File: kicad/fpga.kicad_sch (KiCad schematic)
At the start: 83 parts, among them U1 XC7A50T-2CSG325I

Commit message: Update Odin hardware design, imported parts, and documentation
Include EasyEDA symbols, footprints and 3D models; revise FPGA allocation, power and extension buses; add qualification audits and user documentation.

Validation: EasyEDA audit, qualified parts, power budget and Python syntax pass. KiCad ERC reports 1 error and 319 warnings; DRC reports 90 violations, 499 unconnected items and 209 schematic parity issues. This is a work-in-progress design snapshot. Imported vendor assets retain their original formatting.
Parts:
- added C100, C101, C102, C103, C104, C105, C106, C107, C108, C109, C110, C111, C98, C99: 4.7uF, Capacitor_SMD:C_0603_1608Metric, symbol Device:C
- added C75, C76, C77, C78, C79, C80, C81, C82, C83, C84, C85, C86, C87, C88, C89, C90, C91, C92, C93, C94, C95, C96, C97: 100nF, Capacitor_SMD:C_0402_1005Metric, symbol Device:C
- added unit 8 of U1
- added unit 9 of U1
- added unit 10 of U1
- added unit 11 of U1
- C1, C10, C11, C12, C13, C14, C15, C16, C17, C18, C19, C2, C20, C21, C22, C23, C24, C25, C26, C27, C28, C29, C3, C30, C31, C32, C33, C34, C35, C36, C37, C38, C39, C4, C40, C41, C42, C43, C44, C45, C46, C47, C48, C49, C5, C50, C51, C52, C53, C54, C55, C56, C57, C58, C59, C6, C60, C7, C8, C9: LCSC (none) -> C1525
- C61, C62, C63, C64, C65, C66, C67, C68, C69, C70, C71, C72, C73, C74: value 4.7uF -> 100nF; footprint Capacitor_SMD:C_0603_1608Metric -> Capacitor_SMD:C_0402_1005Metric; LCSC (none) -> C1525
- D1: value green -> F.0603.00025/P2-0603G1TS2-06T-002; footprint LED_SMD:LED_0603_1608Metric -> EasyEDA:LED0603-RD_GREEN; symbol Device:LED -> EasyEDA:F.0603.00025_P2-0603G1TS2-06T-002; LCSC (none) -> C7496818
- R1, R2, R3, R4, R5, R6: LCSC (none) -> C25900
- U1: value XC7A50T-2CSG325I -> XC7A100T-2FGG676I; footprint odin:BGA-324_15x15mm_Layout18x18_P0.8mm -> EasyEDA:FBGA-676_L27.0-W27.0-R26-C26-P1.00-BL; symbol odin:XC7A50T-2CSG325I -> odin:XC7A100T-2FGG676I; LCSC (none) -> C1521803
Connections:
- net +1V0: now also C32.1, C33.1, C34.1, C35.1, C36.1, C37.1, C38.1, C39.1, C40.1, C46.1, C47.1, C48.1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; no longer C11.1, C12.1, C13.1, C14.1, C15.1, C16.1, C17.1, C18.1, C19.1, C20.1, C21.1, C22.1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
- net +1V0_MGT: now also C10.1, C11.1, C12.1, C13.1, C14.1, C15.1, C6.1, C7.1, C8.1, C9.1, C110.1, U1.AA10 (MGTAVCC_G10)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; no longer C32.1, C33.1, C34.1, C35.1, C73.1, U1.B4 (MGTAVCC), U1.C5 (MGTAVCC), U1.E5 (MGTAVCC), U1.F5 (MGTAVCC)
- net +1V2_MGT: now also C16.1, C17.1, C18.1, C19.1, C20.1, C21.1, C22.1, C23.1, C24.1, C25.1, C26.1, C27.1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; no longer C36.1, C37.1, C38.1, C39.1, C40.1, C74.1, U1.A2 (MGTAVTT), U1.C1 (MGTAVTT), U1.E1 (MGTAVTT), U1.F3 (MGTAVTT), U1.G2 (MGTAVTT)
- net +1V8: now also C41.1, C42.1, C43.1, C44.1, C45.1, U1.M12 (VCCADC_0), U1.P12 (VREFP_0), C102.1, C103.1, U1.J9 (VCCAUX), U1.L9 (VCCAUX), U1.N9 (VCCAUX)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; no longer C10.1, C6.1, C65.1, C66.1, C7.1, C8.1, C9.1, U1.G12 (VCCAUX), U1.H13 (VCCAUX), U1.J10 (VCCADC_0), U1.K13 (VCCAUX), U1.L10 (VREFP_0)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
- net +3V3: now also C50.1, C51.1, C52.1, C53.1, C54.1, C55.1, C56.1, C57.1, C58.1, C59.1, C60.1, C61.1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; no longer C41.1, C42.1, C43.1, C44.1, C45.1, C46.1, C47.1, C68.1, U1.E10 (VCCO_0), U1.E12 (CFGBVS_0), U1.L16 (VCCO_14), U1.P17 (VCCO_14)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
- net CFG_CCLK: now also U1.H13 (CCLK_0); no longer U1.E8 (CCLK_0)
- net CFG_DONE: now also U1.W10 (DONE_0); no longer U1.F12 (DONE_0)
- net CFG_INIT_B: now also U1.V11 (INIT_B_0); no longer U1.T10 (INIT_B_0)
- net CFG_M0: now also U1.AB7 (M0_0); no longer U1.R12 (M0_0)
- net CFG_M1: now also U1.Y9 (M1_0); no longer U1.R11 (M1_0)
- net CFG_M2: now also U1.W9 (M2_0); no longer U1.F13 (M2_0)
- net CFG_PROG_B: now also U1.AE16 (PROGRAM_B_0); no longer U1.P10 (PROGRAM_B_0)
- net DBG_TCK: now also U1.P23 (IO_L17P_T2_A14_D30_14); no longer U1.U15 (IO_L17P_T2_A14_D30_14)
- net DBG_TDI: now also U1.R20 (IO_L18P_T2_A12_D28_14); no longer U1.V16 (IO_L18P_T2_A12_D28_14)
- net DBG_TDO: now also U1.R21 (IO_L18N_T2_A11_D27_14); no longer U1.V17 (IO_L18N_T2_A11_D27_14)
- net DBG_TMS: now also U1.P24 (IO_L17N_T2_A13_D29_14); no longer U1.U16 (IO_L17N_T2_A13_D29_14)
- net FLASH_CS_B: now also U1.P18 (IO_L6P_T0_FCS_B_14); no longer U1.L15 (IO_L6P_T0_FCS_B_14)
- net FLASH_D0_MOSI: now also U1.R14 (IO_L1P_T0_D00_MOSI_14); no longer U1.K16 (IO_L1P_T0_D00_MOSI_14)
- net FLASH_D1_MISO: now also U1.R15 (IO_L1N_T0_D01_DIN_14); no longer U1.L17 (IO_L1N_T0_D01_DIN_14)
- net FLASH_D2_WP: now also U1.P14 (IO_L2P_T0_D02_14); no longer U1.J15 (IO_L2P_T0_D02_14)
- net FLASH_D3_HOLD: now also U1.N14 (IO_L2N_T0_D03_14); no longer U1.J16 (IO_L2N_T0_D03_14)
- net FPGA_DXN: now also U1.R11 (DXN_0); no longer U1.M9 (DXN_0)
- net FPGA_DXP: now also U1.R12 (DXP_0); no longer U1.M10 (DXP_0)
- net GND: now also U1.G14 (VCCBATT_0), U1.M11 (GNDADC_0), U1.N11 (VREFN_0), U1.N12 (VP_0), U1.P11 (VN_0), C100.2, C101.2, C102.2, C103.2, C104.2, C105.2, C106.2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; no longer U1.A1 (GND), U1.A11 (GND), U1.A18 (GND), U1.A5 (GND), U1.A7 (GND), U1.A8 (GND), U1.B18 (GND), U1.B3 (GND), U1.B7 (GND), U1.B8 (GND), U1.C15 (GND), U1.C2 (GND)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
- net JTAG_TCK: now also U1.H12 (TCK_0); no longer U1.F8 (TCK_0)
- net JTAG_TDI: now also U1.H10 (TDI_0); no longer U1.T9 (TDI_0)
- net JTAG_TDO: now also U1.J10 (TDO_0); no longer U1.T8 (TDO_0)
- net JTAG_TMS: now also U1.H11 (TMS_0); no longer U1.R8 (TMS_0)
- net MGTPRXN0: now also U1.A11 (MGTPRXN0_216); no longer U1.E3 (MGTPRXN0_216)
- net MGTPRXN1: now also U1.C14 (MGTPRXN1_216); no longer U1.A3 (MGTPRXN1_216)
- net MGTPRXP0: now also U1.B11 (MGTPRXP0_216); no longer U1.E4 (MGTPRXP0_216)
- net MGTPRXP1: now also U1.D14 (MGTPRXP1_216); no longer U1.A4 (MGTPRXP1_216)
- net MGTPTXN0: now also U1.A7 (MGTPTXN0_216); no longer U1.H1 (MGTPTXN0_216)
- net MGTPTXN1: now also U1.C8 (MGTPTXN1_216); no longer U1.F1 (MGTPTXN1_216)
- net MGTPTXP0: now also U1.B7 (MGTPTXP0_216); no longer U1.H2 (MGTPTXP0_216)
- net MGTPTXP1: now also U1.D8 (MGTPTXP1_216); no longer U1.F2 (MGTPTXP1_216)
- net MGTREFCLK0N: now also U1.E11 (MGTREFCLK0N_216); no longer U1.D5 (MGTREFCLK0N_216)
- net MGTREFCLK0P: now also U1.F11 (MGTREFCLK0P_216); no longer U1.D6 (MGTREFCLK0P_216)
- net MGTRREF: now also U1.A15 (MGTRREF_216); no longer U1.A6 (MGTRREF_216)
- net PSRAM0_CE_B: now also U1.N17 (IO_L4N_T0_D05_14); no longer U1.L18 (IO_L4N_T0_D05_14)
- net PSRAM0_IO0: now also U1.R16 (IO_L5P_T0_D06_14); no longer U1.J14 (IO_L5P_T0_D06_14)
- net PSRAM0_IO1: now also U1.R17 (IO_L5N_T0_D07_14); no longer U1.K15 (IO_L5N_T0_D07_14)
- net PSRAM0_IO2: now also U1.K25 (IO_L7P_T1_D09_14); no longer U1.M16 (IO_L7P_T1_D09_14)
- net PSRAM0_IO3: now also U1.K26 (IO_L7N_T1_D10_14); no longer U1.M17 (IO_L7N_T1_D10_14)
- net PSRAM0_SCK: now also U1.N16 (IO_L4P_T0_D04_14); no longer U1.K17 (IO_L4P_T0_D04_14)
- net PSRAM1_CE_B: now also U1.L20 (IO_L8N_T1_D12_14); no longer U1.N14 (IO_L8N_T1_D12_14)
- net PSRAM1_IO0: now also U1.L24 (IO_L9P_T1_DQS_14); no longer U1.N16 (IO_L9P_T1_DQS_14)
- net PSRAM1_IO1: now also U1.L25 (IO_L9N_T1_DQS_D13_14); no longer U1.N17 (IO_L9N_T1_DQS_D13_14)
- net PSRAM1_IO2: now also U1.M24 (IO_L10P_T1_D14_14); no longer U1.N18 (IO_L10P_T1_D14_14)
- net PSRAM1_IO3: now also U1.M25 (IO_L10N_T1_D15_14); no longer U1.P18 (IO_L10N_T1_D15_14)
- net PSRAM1_SCK: now also U1.M20 (IO_L8P_T1_D11_14); no longer U1.M14 (IO_L8P_T1_D11_14)
- net PSRAM2_CE_B: now also U1.L23 (IO_L11N_T1_SRCC_14); no longer U1.P16 (IO_L11N_T1_SRCC_14)
- net PSRAM2_IO0: now also U1.M21 (IO_L12P_T1_MRCC_14); no longer U1.P14 (IO_L12P_T1_MRCC_14)
- net PSRAM2_IO1: now also U1.M22 (IO_L12N_T1_MRCC_14); no longer U1.R15 (IO_L12N_T1_MRCC_14)
- net PSRAM2_IO2: now also U1.N21 (IO_L13P_T2_MRCC_14); no longer U1.T14 (IO_L13P_T2_MRCC_14)
- net PSRAM2_IO3: now also U1.N22 (IO_L13N_T2_MRCC_14); no longer U1.T15 (IO_L13N_T2_MRCC_14)
- net PSRAM2_SCK: now also U1.L22 (IO_L11P_T1_SRCC_14); no longer U1.P15 (IO_L11P_T1_SRCC_14)
- net PSRAM3_CE_B: now also U1.P21 (IO_L14N_T2_SRCC_14); no longer U1.R17 (IO_L14N_T2_SRCC_14)
- net PSRAM3_IO0: now also U1.N23 (IO_L15P_T2_DQS_RDWR_B_14); no longer U1.R18 (IO_L15P_T2_DQS_RDWR_B_14)
- net PSRAM3_IO1: now also U1.N24 (IO_L15N_T2_DQS_DOUT_CSO_B_14); no longer U1.T18 (IO_L15N_T2_DQS_DOUT_CSO_B_14)
- net PSRAM3_IO2: now also U1.P19 (IO_L16P_T2_CSI_B_14); no longer U1.T17 (IO_L16P_T2_CSI_B_14)
- net PSRAM3_IO3: now also U1.N19 (IO_L16N_T2_A15_D31_14); no longer U1.U17 (IO_L16N_T2_A15_D31_14)
- net PSRAM3_SCK: now also U1.P20 (IO_L14P_T2_SRCC_14); no longer U1.R16 (IO_L14P_T2_SRCC_14)
- net PUDC_B: now also U1.P15 (IO_L3P_T0_DQS_PUDC_B_14); no longer U1.J18 (IO_L3P_T0_DQS_PUDC_B_14)
- net SB_UART_RX: now also U1.R25 (IO_L19P_T3_A10_D26_14); no longer U1.R13 (IO_L19P_T3_A10_D26_14)
- net SB_UART_TX: now also U1.P25 (IO_L19N_T3_A09_D25_VREF_14); no longer U1.T13 (IO_L19N_T3_A09_D25_VREF_14)
- net VCCIO_1: now also C68.1, C71.1, C72.1, C73.1, U1.F26 (VCCO_15), U1.G23 (VCCO_15), U1.H20 (VCCO_15), U1.J17 (VCCO_15), U1.K14 (VCCO_15), U1.M18 (VCCO_15), C106.1, C107.1; no longer C48.1, C49.1, C50.1, C51.1, C52.1, C53.1, C54.1, U1.A16 (VCCO_15), U1.B13 (VCCO_15), U1.C10 (VCCO_15), U1.D17 (VCCO_15), U1.E14 (VCCO_15)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
- net VCCIO_2: now also U1.K4 (VCCO_34), U1.L1 (VCCO_34), U1.M8 (VCCO_34), U1.N5 (VCCO_34), U1.P2 (VCCO_34), U1.T6 (VCCO_34), C108.1, C109.1, C86.1, C87.1, C88.1, C89.1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; no longer C55.1, C56.1, C57.1, C58.1, C59.1, C60.1, C71.1, C72.1, U1.L6 (VCCO_34), U1.M3 (VCCO_34), U1.P7 (VCCO_34), U1.R4 (VCCO_34)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
- removed net MGTPRXN2: U1.C3 (MGTPRXN2_216)
- removed net MGTPRXN3: U1.G3 (MGTPRXN3_216)
- removed net MGTPRXP2: U1.C4 (MGTPRXP2_216)
- removed net MGTPRXP3: U1.G4 (MGTPRXP3_216)
- removed net MGTPTXN2: U1.D1 (MGTPTXN2_216)
- removed net MGTPTXN3: U1.B1 (MGTPTXN3_216)
- removed net MGTPTXP2: U1.D2 (MGTPTXP2_216)
- removed net MGTPTXP3: U1.B2 (MGTPTXP3_216)
- removed net MGTREFCLK1N: U1.B5 (MGTREFCLK1N_216)
- removed net MGTREFCLK1P: U1.B6 (MGTREFCLK1P_216)
- removed net SLOTA_P0_N: U1.C8 (IO_L1N_T0_AD0N_15)
- removed net SLOTA_P0_P: U1.D8 (IO_L1P_T0_AD0P_15)
- removed net SLOTA_P1_N: U1.C9 (IO_L2N_T0_AD8N_15)
- removed net SLOTA_P1_P: U1.D9 (IO_L2P_T0_AD8P_15)
- removed net SLOTA_P2_N: U1.A9 (IO_L3N_T0_DQS_AD1N_15)
- removed net SLOTA_P2_P: U1.B9 (IO_L3P_T0_DQS_AD1P_15)
- removed net SLOTA_P3_N: U1.B11 (IO_L4N_T0_15)
- removed net SLOTA_P3_P: U1.C11 (IO_L4P_T0_15)
- removed net SLOTA_P4_N: U1.A10 (IO_L5N_T0_AD9N_15)
- removed net SLOTA_P4_P: U1.B10 (IO_L5P_T0_AD9P_15)
- removed net SLOTB_P0_N: U1.C12 (IO_L6N_T0_VREF_15)
- removed net SLOTB_P0_P: U1.D11 (IO_L6P_T0_15)
- removed net SLOTB_P1_N: U1.A12 (IO_L7N_T1_AD2N_15)
- removed net SLOTB_P1_P: U1.B12 (IO_L7P_T1_AD2P_15)
- removed net SLOTB_P2_N: U1.A14 (IO_L8N_T1_AD10N_15)
- removed net SLOTB_P2_P: U1.A13 (IO_L8P_T1_AD10P_15)
- removed net SLOTB_P3_N: U1.B15 (IO_L9N_T1_DQS_AD3N_15)
- removed net SLOTB_P3_P: U1.C14 (IO_L9P_T1_DQS_AD3P_15)
- removed net SLOTB_P4_N: U1.A15 (IO_L10N_T1_AD11N_15)
- removed net SLOTB_P4_P: U1.B14 (IO_L10P_T1_AD11P_15)
- removed net SLOTC_P0_N: U1.C13 (IO_L11N_T1_SRCC_15)
- removed net SLOTC_P0_P: U1.D13 (IO_L11P_T1_SRCC_15)
- removed net SLOTC_P1_N: U1.D14 (IO_L12N_T1_MRCC_15)
- removed net SLOTC_P1_P: U1.E13 (IO_L12P_T1_MRCC_15)
- removed net SLOTC_P2_N: U1.D15 (IO_L13N_T2_MRCC_15)
- removed net SLOTC_P2_P: U1.E15 (IO_L13P_T2_MRCC_15)
- removed net SLOTC_P3_N: U1.D16 (IO_L14N_T2_SRCC_15)
- removed net SLOTC_P3_P: U1.E16 (IO_L14P_T2_SRCC_15)
- removed net SLOTC_P4_N: U1.A17 (IO_L15N_T2_DQS_ADV_B_15)
- removed net SLOTC_P4_P: U1.B16 (IO_L15P_T2_DQS_15)
- removed net SLOTD_P0_N: U1.B17 (IO_L16N_T2_A27_15)
- removed net SLOTD_P0_P: U1.C16 (IO_L16P_T2_A28_15)
- removed net SLOTD_P1_N: U1.D18 (IO_L17N_T2_A25_15)
- removed net SLOTD_P1_P: U1.E17 (IO_L17P_T2_A26_15)
- removed net SLOTD_P2_N: U1.C18 (IO_L18N_T2_A23_15)
- removed net SLOTD_P2_P: U1.C17 (IO_L18P_T2_A24_15)
- removed net SLOTD_P3_N: U1.F18 (IO_L19N_T3_A21_VREF_15)
- removed net SLOTD_P3_P: U1.G17 (IO_L19P_T3_A22_15)
- removed net SLOTD_P4_N: U1.G16 (IO_L20N_T3_A19_15)
- removed net SLOTD_P4_P: U1.H16 (IO_L20P_T3_A20_15)
- removed net SLOTE_P0_N: U1.K5 (IO_L1N_T0_34)
- removed net SLOTE_P0_P: U1.K6 (IO_L1P_T0_34)
- removed net SLOTE_P1_N: U1.J4 (IO_L2N_T0_34)
- removed net SLOTE_P1_P: U1.J5 (IO_L2P_T0_34)
- removed net SLOTE_P2_N: U1.K1 (IO_L3N_T0_DQS_34)
- removed net SLOTE_P2_P: U1.K2 (IO_L3P_T0_DQS_34)
- removed net SLOTE_P3_N: U1.L2 (IO_L4N_T0_34)
- removed net SLOTE_P3_P: U1.K3 (IO_L4P_T0_34)
- removed net SLOTE_P4_N: U1.L3 (IO_L5N_T0_34)
- removed net SLOTE_P4_P: U1.L4 (IO_L5P_T0_34)
- removed net SLOTF_P0_N: U1.M5 (IO_L6N_T0_VREF_34)
- removed net SLOTF_P0_P: U1.L5 (IO_L6P_T0_34)
- removed net SLOTF_P1_N: U1.M1 (IO_L7N_T1_34)
- removed net SLOTF_P1_P: U1.M2 (IO_L7P_T1_34)
- removed net SLOTF_P2_N: U1.N6 (IO_L8N_T1_34)
- removed net SLOTF_P2_P: U1.M6 (IO_L8P_T1_34)
- removed net SLOTF_P3_N: U1.P1 (IO_L9N_T1_DQS_34)
- removed net SLOTF_P3_P: U1.N1 (IO_L9P_T1_DQS_34)
- removed net SLOTF_P4_N: U1.N4 (IO_L10N_T1_34)
- removed net SLOTF_P4_P: U1.M4 (IO_L10P_T1_34)
- removed net SLOTG_P0_N: U1.N2 (IO_L11N_T1_SRCC_34)
- removed net SLOTG_P0_P: U1.N3 (IO_L11P_T1_SRCC_34)
- removed net SLOTG_P1_N: U1.P3 (IO_L12N_T1_MRCC_34)
- removed net SLOTG_P1_P: U1.P4 (IO_L12P_T1_MRCC_34)
- removed net SLOTG_P2_N: U1.R1 (IO_L13N_T2_MRCC_34)
- removed net SLOTG_P2_P: U1.R2 (IO_L13P_T2_MRCC_34)
- removed net SLOTG_P3_N: U1.T2 (IO_L14N_T2_SRCC_34)
- removed net SLOTG_P3_P: U1.R3 (IO_L14P_T2_SRCC_34)
- removed net SLOTG_P4_N: U1.U1 (IO_L15N_T2_DQS_34)
- removed net SLOTG_P4_P: U1.U2 (IO_L15P_T2_DQS_34)
- removed net SLOTH_P0_N: U1.V2 (IO_L16N_T2_34)
- removed net SLOTH_P0_P: U1.V3 (IO_L16P_T2_34)
- removed net SLOTH_P1_N: U1.T3 (IO_L17N_T2_34)
- removed net SLOTH_P1_P: U1.T4 (IO_L17P_T2_34)
- removed net SLOTH_P2_N: U1.V4 (IO_L18N_T2_34)
- removed net SLOTH_P2_P: U1.U4 (IO_L18P_T2_34)
- removed net SLOTH_P3_N: U1.P5 (IO_L19N_T3_VREF_34)
- removed net SLOTH_P3_P: U1.P6 (IO_L19P_T3_34)
- removed net SLOTH_P4_N: U1.U5 (IO_L20N_T3_34)
- removed net SLOTH_P4_P: U1.U6 (IO_L20P_T3_34)
- removed net SLOTL_DIR0: U1.L14 (IO_0_14)
- removed net SLOTL_DIR1: U1.U10 (IO_25_14)
- net SLOTL_P0_N: no longer names the net of U1.V14 (IO_L23N_T3_13)
- net SLOTL_P0_P: no longer names the net of U1.U14 (IO_L23P_T3_13)
- removed net SLOTL_P1_N: U1.V13 (IO_L21N_T3_DQS_A06_D22_14)
- removed net SLOTL_P1_P: U1.V12 (IO_L21P_T3_DQS_14)
- removed net SLOTL_P2_N: U1.U12 (IO_L22N_T3_A04_D20_14)
- removed net SLOTL_P2_P: U1.T12 (IO_L22P_T3_A05_D21_14)
- removed net SLOTL_P3_N: U1.V11 (IO_L23N_T3_A02_D18_14)
- removed net SLOTL_P3_P: U1.U11 (IO_L23P_T3_A03_D19_14)
- removed net SLOTL_P4_N: U1.V9 (IO_L24N_T3_A00_D16_14)
- removed net SLOTL_P4_P: U1.U9 (IO_L24P_T3_A01_D17_14)
- new net BUS5V0_DIR: U1.M19 (IO_0_14)
- new net BUS5V0_IO0: U1.N26 (IO_L20P_T3_A08_D24_14)
- new net BUS5V0_IO1: U1.M26 (IO_L20N_T3_A07_D23_14)
- new net BUS5V0_IO2: U1.T24 (IO_L21P_T3_DQS_14)
- new net BUS5V0_IO3: U1.T25 (IO_L21N_T3_DQS_A06_D22_14)
- new net BUS5V0_IO4: U1.R26 (IO_L22P_T3_A05_D21_14)
- new net BUS5V0_IO5: U1.P26 (IO_L22N_T3_A04_D20_14)
- new net BUS5V0_IO6: U1.T22 (IO_L23P_T3_A03_D19_14)
- new net BUS5V0_IO7: U1.R22 (IO_L23N_T3_A02_D18_14)
- new net BUS5V1_DIR: U1.U24 (IO_0_13)
- new net BUS5V1_IO0: U1.U25 (IO_L1P_T0_13)
- new net BUS5V1_IO1: U1.U26 (IO_L1N_T0_13)
- new net BUS5V1_IO2: U1.V26 (IO_L2P_T0_13)
- new net BUS5V1_IO3: U1.W26 (IO_L2N_T0_13)
- new net BUS5V1_IO4: U1.AB26 (IO_L3P_T0_DQS_13)
- new net BUS5V1_IO5: U1.AC26 (IO_L3N_T0_DQS_13)
- new net BUS5V1_IO6: U1.W25 (IO_L4P_T0_13)
- new net BUS5V1_IO7: U1.Y26 (IO_L4N_T0_13)
- new net SLOTA_IO0: U1.K15 (IO_L1P_T0_AD0P_15)
- new net SLOTA_IO1: U1.J16 (IO_L1N_T0_AD0N_15)
- new net SLOTA_IO10: U1.M16 (IO_L6P_T0_15)
- new net SLOTA_IO11: U1.M17 (IO_L6N_T0_VREF_15)
- new net SLOTA_IO2: U1.J14 (IO_L2P_T0_AD8P_15)
- new net SLOTA_IO3: U1.J15 (IO_L2N_T0_AD8N_15)
- new net SLOTA_IO4: U1.K16 (IO_L3P_T0_DQS_AD1P_15)
- new net SLOTA_IO5: U1.K17 (IO_L3N_T0_DQS_AD1N_15)
- new net SLOTA_IO6: U1.M14 (IO_L4P_T0_15)
- new net SLOTA_IO7: U1.L14 (IO_L4N_T0_15)
- new net SLOTA_IO8: U1.M15 (IO_L5P_T0_AD9P_15)
- new net SLOTA_IO9: U1.L15 (IO_L5N_T0_AD9N_15)
- new net SLOTB_IO0: U1.J19 (IO_L7P_T1_AD2P_15)
- new net SLOTB_IO1: U1.H19 (IO_L7N_T1_AD2N_15)
- new net SLOTB_IO10: U1.K21 (IO_L12P_T1_MRCC_15)
- new net SLOTB_IO11: U1.J21 (IO_L12N_T1_MRCC_15)
- new net SLOTB_IO2: U1.L17 (IO_L8P_T1_AD10P_15)
- new net SLOTB_IO3: U1.L18 (IO_L8N_T1_AD10N_15)
- new net SLOTB_IO4: U1.K20 (IO_L9P_T1_DQS_AD3P_15)
- new net SLOTB_IO5: U1.J20 (IO_L9N_T1_DQS_AD3N_15)
- new net SLOTB_IO6: U1.J18 (IO_L10P_T1_AD11P_15)
- new net SLOTB_IO7: U1.H18 (IO_L10N_T1_AD11N_15)
- new net SLOTB_IO8: U1.G20 (IO_L11P_T1_SRCC_15)
- new net SLOTB_IO9: U1.G21 (IO_L11N_T1_SRCC_15)
- new net SLOTC_IO0: U1.H21 (IO_L13P_T2_MRCC_15)
- new net SLOTC_IO1: U1.H22 (IO_L13N_T2_MRCC_15)
- new net SLOTC_IO10: U1.K22 (IO_L18P_T2_A24_15)
- new net SLOTC_IO11: U1.K23 (IO_L18N_T2_A23_15)
- new net SLOTC_IO2: U1.J23 (IO_L14P_T2_SRCC_15)
- new net SLOTC_IO3: U1.H23 (IO_L14N_T2_SRCC_15)
- new net SLOTC_IO4: U1.G22 (IO_L15P_T2_DQS_15)
- new net SLOTC_IO5: U1.F22 (IO_L15N_T2_DQS_ADV_B_15)
- new net SLOTC_IO6: U1.J24 (IO_L16P_T2_A28_15)
- new net SLOTC_IO7: U1.H24 (IO_L16N_T2_A27_15)
- new net SLOTC_IO8: U1.F23 (IO_L17P_T2_A26_15)
- new net SLOTC_IO9: U1.E23 (IO_L17N_T2_A25_15)
- new net SLOTD_IO0: U1.G24 (IO_L19P_T3_A22_15)
- new net SLOTD_IO1: U1.F24 (IO_L19N_T3_A21_VREF_15)
- new net SLOTD_IO10: U1.J25 (IO_L24P_T3_RS1_15)
- new net SLOTD_IO11: U1.J26 (IO_L24N_T3_RS0_15)
- new net SLOTD_IO2: U1.E25 (IO_L20P_T3_A20_15)
- new net SLOTD_IO3: U1.D25 (IO_L20N_T3_A19_15)
- new net SLOTD_IO4: U1.E26 (IO_L21P_T3_DQS_15)
- new net SLOTD_IO5: U1.D26 (IO_L21N_T3_DQS_A18_15)
- new net SLOTD_IO6: U1.H26 (IO_L22P_T3_A17_15)
- new net SLOTD_IO7: U1.G26 (IO_L22N_T3_A16_15)
- new net SLOTD_IO8: U1.G25 (IO_L23P_T3_FOE_B_15)
- new net SLOTD_IO9: U1.F25 (IO_L23N_T3_FWE_B_15)
- new net SLOTE_IO0: U1.K3 (IO_L1P_T0_34)
- new net SLOTE_IO1: U1.J3 (IO_L1N_T0_34)
- new net SLOTE_IO10: U1.M6 (IO_L6P_T0_34)
- new net SLOTE_IO11: U1.M5 (IO_L6N_T0_VREF_34)
- new net SLOTE_IO2: U1.M7 (IO_L2P_T0_34)
- new net SLOTE_IO3: U1.L7 (IO_L2N_T0_34)
- new net SLOTE_IO4: U1.M4 (IO_L3P_T0_DQS_34)
- new net SLOTE_IO5: U1.L4 (IO_L3N_T0_DQS_34)
- new net SLOTE_IO6: U1.L5 (IO_L4P_T0_34)
- new net SLOTE_IO7: U1.K5 (IO_L4N_T0_34)
- new net SLOTE_IO8: U1.N7 (IO_L5P_T0_34)
- new net SLOTE_IO9: U1.N6 (IO_L5N_T0_34)
- new net SLOTF_IO0: U1.K1 (IO_L7P_T1_34)
- new net SLOTF_IO1: U1.J1 (IO_L7N_T1_34)
- new net SLOTF_IO10: U1.N3 (IO_L12P_T1_MRCC_34)
- new net SLOTF_IO11: U1.N2 (IO_L12N_T1_MRCC_34)
- new net SLOTF_IO2: U1.L3 (IO_L8P_T1_34)
- new net SLOTF_IO3: U1.K2 (IO_L8N_T1_34)
- new net SLOTF_IO4: U1.N1 (IO_L9P_T1_DQS_34)
- new net SLOTF_IO5: U1.M1 (IO_L9N_T1_DQS_34)
- new net SLOTF_IO6: U1.H2 (IO_L10P_T1_34)
- new net SLOTF_IO7: U1.H1 (IO_L10N_T1_34)
- new net SLOTF_IO8: U1.M2 (IO_L11P_T1_SRCC_34)
- new net SLOTF_IO9: U1.L2 (IO_L11N_T1_SRCC_34)
- new net SLOTG_IO0: U1.R3 (IO_L13P_T2_MRCC_34)
- new net SLOTG_IO1: U1.P3 (IO_L13N_T2_MRCC_34)
- new net SLOTG_IO10: U1.U2 (IO_L18P_T2_34)
- new net SLOTG_IO11: U1.U1 (IO_L18N_T2_34)
- new net SLOTG_IO2: U1.P4 (IO_L14P_T2_SRCC_34)
- new net SLOTG_IO3: U1.N4 (IO_L14N_T2_SRCC_34)
- new net SLOTG_IO4: U1.R1 (IO_L15P_T2_DQS_34)
- new net SLOTG_IO5: U1.P1 (IO_L15N_T2_DQS_34)
- new net SLOTG_IO6: U1.T4 (IO_L16P_T2_34)
- new net SLOTG_IO7: U1.T3 (IO_L16N_T2_34)
- new net SLOTG_IO8: U1.T2 (IO_L17P_T2_34)
- new net SLOTG_IO9: U1.R2 (IO_L17N_T2_34)
- new net SLOTH_IO0: U1.P6 (IO_L19P_T3_34)
- new net SLOTH_IO1: U1.P5 (IO_L19N_T3_VREF_34)
- new net SLOTH_IO10: U1.T8 (IO_L24P_T3_34)
- new net SLOTH_IO11: U1.T7 (IO_L24N_T3_34)
- new net SLOTH_IO2: U1.T5 (IO_L20P_T3_34)
- new net SLOTH_IO3: U1.R5 (IO_L20N_T3_34)
- new net SLOTH_IO4: U1.U6 (IO_L21P_T3_DQS_34)
- new net SLOTH_IO5: U1.U5 (IO_L21N_T3_DQS_34)
- new net SLOTH_IO6: U1.R8 (IO_L22P_T3_34)
- new net SLOTH_IO7: U1.P8 (IO_L22N_T3_34)
- new net SLOTH_IO8: U1.R7 (IO_L23P_T3_34)
- new net SLOTH_IO9: U1.R6 (IO_L23N_T3_34)
- no-connect marks 22 -> 281
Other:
- note added: "FPGA — FPGA, decoupling and configuration straps — HW 0.1.0-proto.1"
- note removed: "FPGA — FPGA, decoupling and configuration straps"
- moved on the sheet: C1, C10, C11, C12, C13, C14, C15, C16, C17, C18, C19, C2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

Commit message: wip
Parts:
- removed C111: 4.7uF, Capacitor_SMD:C_0603_1608Metric, symbol Device:C
- added Q4: BSS138LT1G, EasyEDA:SOT-23-3_L2.9-W1.6-P1.90-LS2.8-BR, symbol Transistor_FET:Q_NMOS_GSD
- added R98: 4.7k, Resistor_SMD:R_0402_1005Metric, symbol Device:R
- C97: value 100nF -> 4.7uF; footprint Capacitor_SMD:C_0402_1005Metric -> Capacitor_SMD:C_0603_1608Metric; LCSC C1525 -> C277476
- R6: value 4.7k -> 1k; LCSC C25900 -> C11702
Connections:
- net +1V0: now also C27.1, C45.1, C97.1; no longer C101.1, C40.1, C49.1
- net +1V0_MGT: now also C109.1, C5.1; no longer C110.1, C15.1
- net +1V2_MGT: now also C110.1, C15.1; no longer C27.1
- net +1V8: now also C101.1, C40.1; no longer C103.1, C2.1, C45.1, U1.P12 (VREFP_0)
- net +3V3: now also C103.1, C2.1, C49.1, C73.1, C91.1, R7.1, R98.1; no longer C105.1, C5.1, C67.1, C85.1, C97.1
- net CFG_DONE: now also Q4.1 (G), R98.2; no longer R7.1
- net GND: now also U1.A13 (MGTPRXN2_216), U1.AC12 (MGTPRXP0_213), U1.AC14 (MGTPRXP2_213), U1.AD12 (MGTPRXN0_213), U1.AD14 (MGTPRXN2_213), U1.AE11 (MGTPRXP3_213), U1.AE13 (MGTPRXP1_213), U1.AF11 (MGTPRXN3_213), U1.AF13 (MGTPRXN1_213), U1.B13 (MGTPRXP2_216), U1.C12 (MGTPRXN3_216), U1.D12 (MGTPRXP3_216), U1.P12 (VREFP_0), Q4.2 (S); no longer D1.1 (C)
- net VCCIO_1: now also C105.1, C67.1; no longer C107.1, C73.1
- net VCCIO_2: now also C107.1, C85.1; no longer C109.1, C91.1
- net MGTRREF_213: now reaches U1.AF15 (MGTRREF_213)
- net BUS5V0_OE_N: now reaches U1.P16 (IO_L3N_T0_DQS_EMCCLK_14)
- net BUS5V1_OE_N: now reaches U1.Y25 (IO_L5P_T0_13)
- new net DONE_LED_K: D1.1 (C), Q4.3 (D)
- no-connect marks 281 -> 266
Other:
- moved on the sheet: C10, C100, C101, C102, C103, C104, C105, C106, C107, C108, C109, C11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

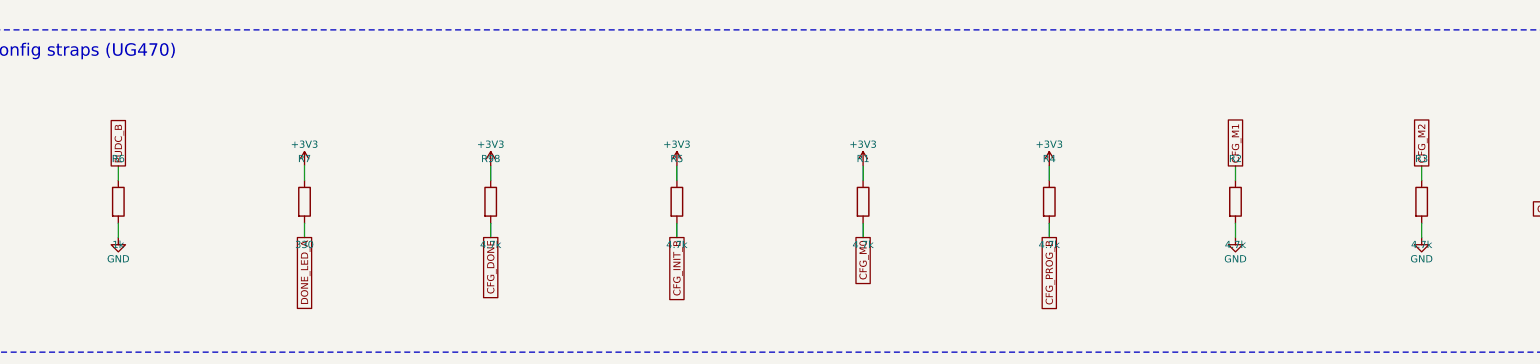
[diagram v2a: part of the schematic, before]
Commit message: Mode straps to 1 k, drop the bottom-side decoupling rule, add depth and gate tools
UG470 Table 2-4 wants the M[2:0] straps at 1 k or less. The board is
assembled on one side, so place.py no longer flips the FPGA decoupling to
B.Cu. tools/depth.py reports the escape depth of every assigned U1 ball and
tools/gate.py runs the per-phase checks and prints the report numbers.
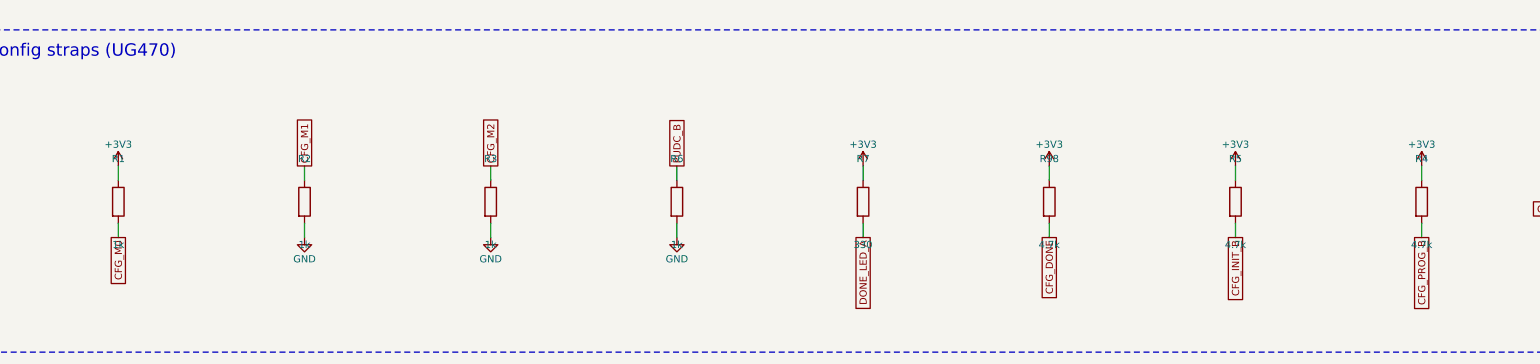
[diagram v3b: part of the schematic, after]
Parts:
- R1, R2, R3: value 4.7k -> 1k; LCSC C25900 -> C11702
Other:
- moved on the sheet: R1, R2, R3, R4, R5, R6, R7, R98

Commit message: FPGA decoupling per UG483 Table 2-2, and stage new footprints below the staged ones
The XC7A100T-FGG676 decoupling network is now the one UG483 v1.14
prescribes for this device and package, in the Table 2-5 bodies: a 330 uF
D-case tantalum, 1210 and 0805 ceramics and 0.47 uF 0603s per supply and
per I/O bank, with one 47 uF per voltage group of up to four VCCO banks.
MGTAVCC/MGTAVTT (UG482's) and VCCADC keep their 100 nF per ball. 92
parts replace the 110 of the one-100nF-per-ball scheme. The new parts take
refs C301..C392 so they do not inherit the script-made 0402 positions
around U1; reserve() keeps every later C ref where it was placed.
ref/decoupling.md records the tables and the placement rule.

load_pcb.py started its import band at a fixed y and stacked new parts on
footprints staged there by earlier imports; it now starts below the lowest
existing footprint. The README no longer claims it discards placement.
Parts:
- removed C1, C10, C11, C12, C13, C14, C15, C16, C17, C18, C19, C2, C20, C21, C22, C23, C24, C25, C26, C27, C28, C29, C3, C30, C31, C32, C33, C34, C35, C36, C37, C38, C39, C4, C40, C41, C42, C43, C44, C45, C46, C47, C48, C49, C5, C50, C51, C52, C53, C54, C55, C56, C57, C58, C59, C6, C60, C61, C62, C63, C64, C65, C66, C67, C68, C69, C7, C70, C71, C72, C73, C74, C75, C76, C77, C78, C79, C8, C80, C81, C82, C83, C84, C85, C86, C87, C88, C89, C9, C90, C91, C92, C93, C94, C95, C96: 100nF, Capacitor_SMD:C_0402_1005Metric, symbol Device:C
- removed C100, C101, C102, C103, C104, C105, C106, C107, C108, C109, C110, C97, C98, C99: 4.7uF, Capacitor_SMD:C_0603_1608Metric, symbol Device:C
- added C301: 330uF 2.5V T520V337M2R5ATE025, Capacitor_Tantalum_SMD:CP_EIA-7343-31_Kemet-D, symbol Device:C_Polarized
- added C302, C303, C304, C305, C306, C307, C320, C321, C322, C330, C331, C336, C337, C342, C343, C348, C349, C354, C355, C360, C361: 4.7uF 6.3V, Capacitor_SMD:C_0805_2012Metric, symbol Device:C
- added C308, C309, C310, C311, C312, C313, C314, C315, C317, C318, C323, C324, C325, C326, C327, C332, C333, C334, C335, C338, C339, C340, C341, C344, C345, C346, C347, C350, C351, C352, C353, C356, C357, C358, C359, C362, C363, C364, C365: 0.47uF 6.3V, Capacitor_SMD:C_0603_1608Metric, symbol Device:C
- added C316: 100uF 2.5V, Capacitor_SMD:C_1210_3225Metric, symbol Device:C
- added C319, C329, C366, C367, C368: 47uF 6.3V, Capacitor_SMD:C_1210_3225Metric, symbol Device:C
- added C328, C369, C370, C371, C372, C373, C374, C375, C376, C377, C378, C379, C380, C381, C382, C383, C384, C385, C386, C387, C388, C389, C390: 100nF, Capacitor_SMD:C_0402_1005Metric, symbol Device:C
- added C391, C392: 4.7uF, Capacitor_SMD:C_0603_1608Metric, symbol Device:C
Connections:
- net +1V0: now also C301.1, C302.1, C303.1, C304.1, C305.1, C306.1, C307.1, C308.1, C309.1, C310.1, C311.1, C312.1, C313.1, C314.1, C315.1, C316.1, C317.1, C318.1
- net +1V0_MGT: now also C369.1, C370.1, C371.1, C372.1, C373.1, C374.1, C375.1, C376.1, C377.1, C378.1, C391.1
- net +1V2_MGT: now also C379.1, C380.1, C381.1, C382.1, C383.1, C384.1, C385.1, C386.1, C387.1, C388.1, C389.1, C390.1, C392.1
- net +1V8: now also C319.1, C320.1, C321.1, C322.1, C323.1, C324.1, C325.1, C326.1, C327.1, C328.1
- net +3V3: now also C329.1, C330.1, C331.1, C332.1, C333.1, C334.1, C335.1, C336.1, C337.1, C338.1, C339.1, C340.1, C341.1, C348.1, C349.1, C350.1, C351.1, C352.1, C353.1, C360.1, C361.1, C362.1, C363.1, C364.1, C365.1, C366.1
- net GND: now also C301.2, C302.2, C303.2, C304.2, C305.2, C306.2, C307.2, C308.2, C309.2, C310.2, C311.2, C312.2, C313.2, C314.2, C315.2, C316.2, C317.2, C318.2, C319.2, C320.2, C321.2, C322.2, C323.2, C324.2, C325.2, C326.2, C327.2, C328.2, C329.2, C330.2, C331.2, C332.2, C333.2, C334.2, C335.2, C336.2, C337.2, C338.2, C339.2, C340.2, C341.2, C342.2, C343.2, C344.2, C345.2, C346.2, C347.2, C348.2, C349.2, C350.2, C351.2, C352.2, C353.2, C354.2, C355.2, C356.2, C357.2, C358.2, C359.2, C360.2, C361.2, C362.2, C363.2, C364.2, C365.2, C366.2, C367.2, C368.2, C369.2, C370.2, C371.2, C372.2, C373.2, C374.2, C375.2, C376.2, C377.2, C378.2, C379.2, C380.2, C381.2, C382.2, C383.2, C384.2, C385.2, C386.2, C387.2, C388.2, C389.2, C390.2, C391.2, C392.2
- net VCCIO_1: now also C342.1, C343.1, C344.1, C345.1, C346.1, C347.1, C367.1
- net VCCIO_2: now also C354.1, C355.1, C356.1, C357.1, C358.1, C359.1, C368.1
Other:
- note added: "decap +1V0_MGT"
- note added: "decap +1V2_MGT"
- note added: "decap VCCADC"
- note added: "decap VCCAUX"
- note added: "decap VCCBRAM"
- note added: "decap VCCINT"
- note added: "decap VCCO group +3V3"
- note added: "decap VCCO group VCCIO_1"
- note added: "decap VCCO group VCCIO_2"
- note added: "decap VCCO_0"
- note added: "decap VCCO_13"
- note added: "decap VCCO_14"
- note added: "decap VCCO_15"
- note added: "decap VCCO_16"
- note added: "decap VCCO_34"
- note added: "decap VCCO_35"
- note removed: "bulk +1V0"
- note removed: "bulk +1V0_MGT"
- note removed: "bulk +1V2_MGT"
- note removed: "bulk +1V8"
- note removed: "bulk +3V3"
- note removed: "bulk VCCIO_1"
- note removed: "bulk VCCIO_2"
- note removed: "decoupling +1V0"
- note removed: "decoupling +1V0_MGT"
- note removed: "decoupling +1V2_MGT"
- note removed: "decoupling +1V8"
- note removed: "decoupling +3V3"
- note removed: "decoupling VCCIO_1"
- note removed: "decoupling VCCIO_2"
- moved on the sheet: D1, Q4, R1, R2, R3, R4, R5, R6, R7, R98

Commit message: Fast Links out, Network in: RTL8211FD-CG on RGMII, ETH jack, LINK P and LINK Q
The two SFP ports, their cages, the 125 MHz oscillator, the power gate and
the I2C switch leave the design, and with them the SFP nets on the board
controller (GPIO32-39 and 46 are spare, GPIO14/31 carry the status expander's
I2C). Both GTP quads stay powered per UG482 with grounded RX and one RCAL
each.

A Network sheet replaces them: an RTL8211FD-CG gigabit PHY on RGMII at 2.5 V
with its straps, reset, interrupt, MDIO pull-up, crystal and jack LEDs wired
from the datasheet rev 1.7 tables, a HanRun HR911130A 1000Base-T magjack,
and two plain shielded 8P8C jacks that carry eight DC-coupled LVDS_25 pairs
from bank 16 with ESD arrays at the jacks. The five new parts came in through
easyeda2kicad; two footprints the importer had shared with other parts got
their own copies, and the jacks' mounting holes are NPTH.

Bank 16 moves to +2V5 and tools/alloc.py allocates it shallowest-first with
the PHY receive clock on an MRCC ball and the two link receive clocks on
clock-capable pairs; both 5 V buses and the PHY control pins live in bank 13;
banks 13, 14 and 16 are depth sorted. Escape depth >= 7 drops from 58 to 50
balls. Docs: ref/network.md and ref/link-ports.md are new; the SFP pages are
gone; status LEDs, user manual, keep-outs and import checklist follow.
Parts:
- added C393: 4.7uF, Capacitor_SMD:C_0603_1608Metric, symbol Device:C
- added R35, R89: 100 1%, Resistor_SMD:R_0603_1608Metric, symbol Device:R
- C369: value 100nF -> 47uF 6.3V; footprint Capacitor_SMD:C_0402_1005Metric -> Capacitor_SMD:C_1210_3225Metric; LCSC C1525 -> (none)
- C391: value 4.7uF -> 100nF; footprint Capacitor_SMD:C_0603_1608Metric -> Capacitor_SMD:C_0402_1005Metric; LCSC C277476 -> C1525
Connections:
- net MGTPRXN0 is gone; now on net GND: U1.A11 (MGTPRXN0_216)
- net MGTPRXN1 is gone; now on net GND: U1.C14 (MGTPRXN1_216)
- net MGTPRXP0 is gone; now on net GND: U1.B11 (MGTPRXP0_216)
- net MGTPRXP1 is gone; now on net GND: U1.D14 (MGTPRXP1_216)
- net +1V0_MGT: now also C379.1, C392.1; no longer C369.1, C391.1
- net +1V2_MGT: now also C391.1, C393.1, R35.2, R89.2; no longer C379.1, C392.1
- net +3V3: no longer C348.1, C349.1, C350.1, C351.1, C352.1, C353.1, U1.A21 (VCCO_16), U1.B18 (VCCO_16), U1.C25 (VCCO_16), U1.D22 (VCCO_16), U1.E19 (VCCO_16), U1.F16 (VCCO_16)
- net BUS5V0_DIR: now also U1.U24 (IO_0_13); no longer U1.M19 (IO_0_14)
- net BUS5V0_IO0: now also U1.V26 (IO_L2P_T0_13); no longer U1.N26 (IO_L20P_T3_A08_D24_14)
- net BUS5V0_IO1: now also U1.W26 (IO_L2N_T0_13); no longer U1.M26 (IO_L20N_T3_A07_D23_14)
- net BUS5V0_IO2: now also U1.AB26 (IO_L3P_T0_DQS_13); no longer U1.T24 (IO_L21P_T3_DQS_14)
- net BUS5V0_IO3: now also U1.AC26 (IO_L3N_T0_DQS_13); no longer U1.T25 (IO_L21N_T3_DQS_A06_D22_14)
- net BUS5V0_IO4: now also U1.U25 (IO_L1P_T0_13); no longer U1.R26 (IO_L22P_T3_A05_D21_14)
- net BUS5V0_IO5: now also U1.U26 (IO_L1N_T0_13); no longer U1.P26 (IO_L22N_T3_A04_D20_14)
- net BUS5V0_IO6: now also U1.W25 (IO_L4P_T0_13); no longer U1.T22 (IO_L23P_T3_A03_D19_14)
- net BUS5V0_IO7: now also U1.Y26 (IO_L4N_T0_13); no longer U1.R22 (IO_L23N_T3_A02_D18_14)
- net BUS5V0_OE_N: now also U1.V23 (IO_L10P_T1_13); no longer U1.P16 (IO_L3N_T0_DQS_EMCCLK_14)
- net BUS5V1_DIR: now also U1.U17 (IO_25_13); no longer U1.U24 (IO_0_13)
- net BUS5V1_IO0: now also U1.Y25 (IO_L5P_T0_13); no longer U1.U25 (IO_L1P_T0_13)
- net BUS5V1_IO1: now also U1.AA25 (IO_L5N_T0_13); no longer U1.U26 (IO_L1N_T0_13)
- net BUS5V1_IO2: now also U1.V24 (IO_L6P_T0_13); no longer U1.V26 (IO_L2P_T0_13)
- net BUS5V1_IO3: now also U1.W24 (IO_L6N_T0_VREF_13); no longer U1.W26 (IO_L2N_T0_13)
- net BUS5V1_IO4: now also U1.AA24 (IO_L7P_T1_13); no longer U1.AB26 (IO_L3P_T0_DQS_13)
- net BUS5V1_IO5: now also U1.AB25 (IO_L7N_T1_13); no longer U1.AC26 (IO_L3N_T0_DQS_13)
- net BUS5V1_IO6: now also U1.AB24 (IO_L9P_T1_DQS_13); no longer U1.W25 (IO_L4P_T0_13)
- net BUS5V1_IO7: now also U1.AC24 (IO_L9N_T1_DQS_13); no longer U1.Y26 (IO_L4N_T0_13)
- net BUS5V1_OE_N: now also U1.W23 (IO_L10N_T1_13); no longer U1.Y25 (IO_L5P_T0_13)
- net DBG_TCK: now also U1.M21 (IO_L12P_T1_MRCC_14); no longer U1.P23 (IO_L17P_T2_A14_D30_14)
- net DBG_TDI: now also U1.N21 (IO_L13P_T2_MRCC_14); no longer U1.R20 (IO_L18P_T2_A12_D28_14)
- net DBG_TDO: now also U1.N22 (IO_L13N_T2_MRCC_14); no longer U1.R21 (IO_L18N_T2_A11_D27_14)
- net DBG_TMS: now also U1.M22 (IO_L12N_T1_MRCC_14); no longer U1.P24 (IO_L17N_T2_A13_D29_14)
- net GND: now also C393.2
- net MGTRREF: now also R35.1
- net MGTRREF_213: now also R89.1
- net PSRAM0_CE_B: now also U1.M26 (IO_L20N_T3_A07_D23_14); no longer U1.N17 (IO_L4N_T0_D05_14)
- net PSRAM0_IO0: now also U1.R26 (IO_L22P_T3_A05_D21_14); no longer U1.R16 (IO_L5P_T0_D06_14)
- net PSRAM0_IO1: now also U1.P26 (IO_L22N_T3_A04_D20_14); no longer U1.R17 (IO_L5N_T0_D07_14)
- net PSRAM0_SCK: now also U1.N26 (IO_L20P_T3_A08_D24_14); no longer U1.N16 (IO_L4P_T0_D04_14)
- net PSRAM1_CE_B: now also U1.P25 (IO_L19N_T3_A09_D25_VREF_14); no longer U1.L20 (IO_L8N_T1_D12_14)
- net PSRAM1_SCK: now also U1.R25 (IO_L19P_T3_A10_D26_14); no longer U1.M20 (IO_L8P_T1_D11_14)
- net PSRAM2_CE_B: now also U1.T25 (IO_L21N_T3_DQS_A06_D22_14); no longer U1.L23 (IO_L11N_T1_SRCC_14)
- net PSRAM2_IO0: now also U1.N23 (IO_L15P_T2_DQS_RDWR_B_14); no longer U1.M21 (IO_L12P_T1_MRCC_14)
- net PSRAM2_IO1: now also U1.N24 (IO_L15N_T2_DQS_DOUT_CSO_B_14); no longer U1.M22 (IO_L12N_T1_MRCC_14)
- net PSRAM2_IO2: now also U1.P23 (IO_L17P_T2_A14_D30_14); no longer U1.N21 (IO_L13P_T2_MRCC_14)
- net PSRAM2_IO3: now also U1.P24 (IO_L17N_T2_A13_D29_14); no longer U1.N22 (IO_L13N_T2_MRCC_14)
- net PSRAM2_SCK: now also U1.T24 (IO_L21P_T3_DQS_14); no longer U1.L22 (IO_L11P_T1_SRCC_14)
- net PSRAM3_CE_B: now also U1.R23 (IO_L24N_T3_A00_D16_14); no longer U1.P21 (IO_L14N_T2_SRCC_14)
- net PSRAM3_IO0: now also U1.L22 (IO_L11P_T1_SRCC_14); no longer U1.N23 (IO_L15P_T2_DQS_RDWR_B_14)
- net PSRAM3_IO1: now also U1.L23 (IO_L11N_T1_SRCC_14); no longer U1.N24 (IO_L15N_T2_DQS_DOUT_CSO_B_14)
- net PSRAM3_IO2: now also U1.T22 (IO_L23P_T3_A03_D19_14); no longer U1.P19 (IO_L16P_T2_CSI_B_14)
- net PSRAM3_IO3: now also U1.R22 (IO_L23N_T3_A02_D18_14); no longer U1.N19 (IO_L16N_T2_A15_D31_14)
- net PSRAM3_SCK: now also U1.T23 (IO_L24P_T3_A01_D17_14); no longer U1.P20 (IO_L14P_T2_SRCC_14)
- net SB_UART_RX: now also U1.M20 (IO_L8P_T1_D11_14); no longer U1.R25 (IO_L19P_T3_A10_D26_14)
- net SB_UART_TX: now also U1.L20 (IO_L8N_T1_D12_14); no longer U1.P25 (IO_L19N_T3_A09_D25_VREF_14)
- net VCCIO_2: now also C369.1; no longer C368.1
- net LINK_P_RXD_P: now reaches U1.A17 (IO_L9P_T1_DQS_16)
- net LINK_P_RXD_N: now reaches U1.A18 (IO_L9N_T1_DQS_16)
- net PHY_RX_CTL: now reaches U1.A19 (IO_L10N_T1_16)
- net LINK_Q_RXD_N: now reaches U1.A20 (IO_L15N_T2_DQS_16)
- net LINK_Q_TXD_N: now reaches U1.A22 (IO_L17N_T2_16)
- net LINK_P_TXD_P: now reaches U1.A23 (IO_L21P_T3_DQS_16)
- net LINK_P_TXD_N: now reaches U1.A24 (IO_L21N_T3_DQS_16)
- net LINK_Q_TXC_N: now reaches U1.A25 (IO_L20N_T3_16)
- net PHY_MDIO: now reaches U1.B17 (IO_L7N_T1_16)
- net PHY_RXD3: now reaches U1.B19 (IO_L10P_T1_16)
- net LINK_Q_RXD_P: now reaches U1.B20 (IO_L15P_T2_DQS_16)
- net PHY_TX_CTL: now reaches U1.B21 (IO_L16N_T2_16)
- net LINK_Q_TXD_P: now reaches U1.B22 (IO_L17P_T2_16)
- net PHY_TXD0: now reaches U1.B24 (IO_L23N_T3_16)
- net LINK_Q_TXC_P: now reaches U1.B25 (IO_L20P_T3_16)
- net LINK_P_TXC_N: now reaches U1.B26 (IO_L22N_T3_16)
- net PHY_MDC: now reaches U1.C17 (IO_L7P_T1_16)
- net LINK_P_RXC_N: now reaches U1.C18 (IO_L12N_T1_MRCC_16)
- net PHY_RXD0: now reaches U1.C19 (IO_L13N_T2_MRCC_16)
- net PHY_TXD3: now reaches U1.C21 (IO_L16P_T2_16)
- net PHY_TXD1: now reaches U1.C22 (IO_L19P_T3_16)
- net PHY_TXD2: now reaches U1.C23 (IO_L19N_T3_VREF_16)
- net PHY_TXC: now reaches U1.C24 (IO_L23P_T3_16)
- net LINK_P_TXC_P: now reaches U1.C26 (IO_L22P_T3_16)
- net LINK_P_RXC_P: now reaches U1.D18 (IO_L12P_T1_MRCC_16)
- net PHY_RXC: now reaches U1.D19 (IO_L13P_T2_MRCC_16)
- net LINK_Q_RXC_N: now reaches U1.D20 (IO_L14N_T2_SRCC_16)
- net LINK_Q_RXC_P: now reaches U1.E20 (IO_L14P_T2_SRCC_16)
- net PHY_RXD2: now reaches U1.E22 (IO_25_16)
- net PHY_RXD1: now reaches U1.H17 (IO_0_16)
- net PHY_RESET_N: now reaches U1.AA22 (IO_L8P_T1_13)
- net PHY_INT_N: now reaches U1.AA23 (IO_L8N_T1_13)
- net MGTPTXN0: no longer names the net of U1.A7 (MGTPTXN0_216)
- net MGTPTXN1: no longer names the net of U1.C8 (MGTPTXN1_216)
- net MGTPTXP0: no longer names the net of U1.B7 (MGTPTXP0_216)
- net MGTPTXP1: no longer names the net of U1.D8 (MGTPTXP1_216)
- net MGTREFCLK0N: no longer names the net of U1.E11 (MGTREFCLK0N_216)
- net MGTREFCLK0P: no longer names the net of U1.F11 (MGTREFCLK0P_216)
- new net +2V5: C348.1, C349.1, C350.1, C351.1, C352.1, C353.1, C368.1, U1.A21 (VCCO_16), U1.B18 (VCCO_16), U1.C25 (VCCO_16), U1.D22 (VCCO_16), U1.E19 (VCCO_16), U1.F16 (VCCO_16)
- no-connect marks 266 -> 240
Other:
- note added: "GTP calibration"
- note added: "decap VCCO group +2V5"
- moved on the sheet: C369, C370, C371, C372, C373, C374, C375, C376, C377, C378, C379, C380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
